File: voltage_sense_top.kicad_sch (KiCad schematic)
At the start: 42 parts, among them IC1 DAC101C081CIMK_NOPB, J1 Conn_Coaxial, J2 Conn_01x04, J4 HDMI_A, J5 Conn_Coaxial, U1 OPA188xxDBV, U2 ADA4000-1, U3 OPA188xxDBV, U4 MCP4017T-103E_LT, U5 OPA1641

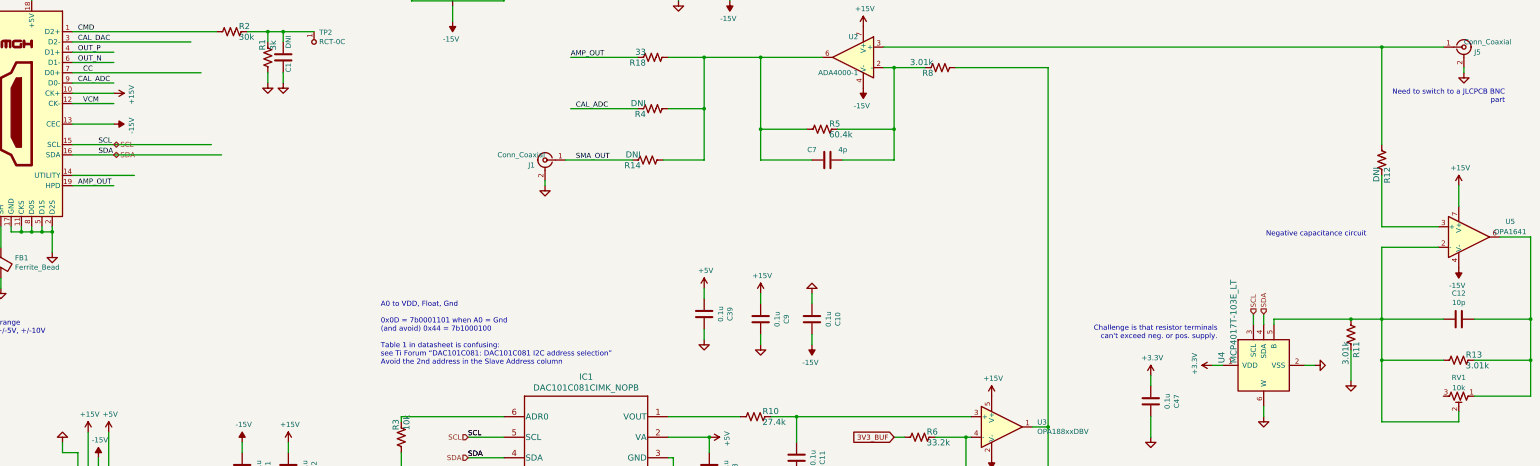
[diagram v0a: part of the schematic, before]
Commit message: found LCSC alternatives for some parts
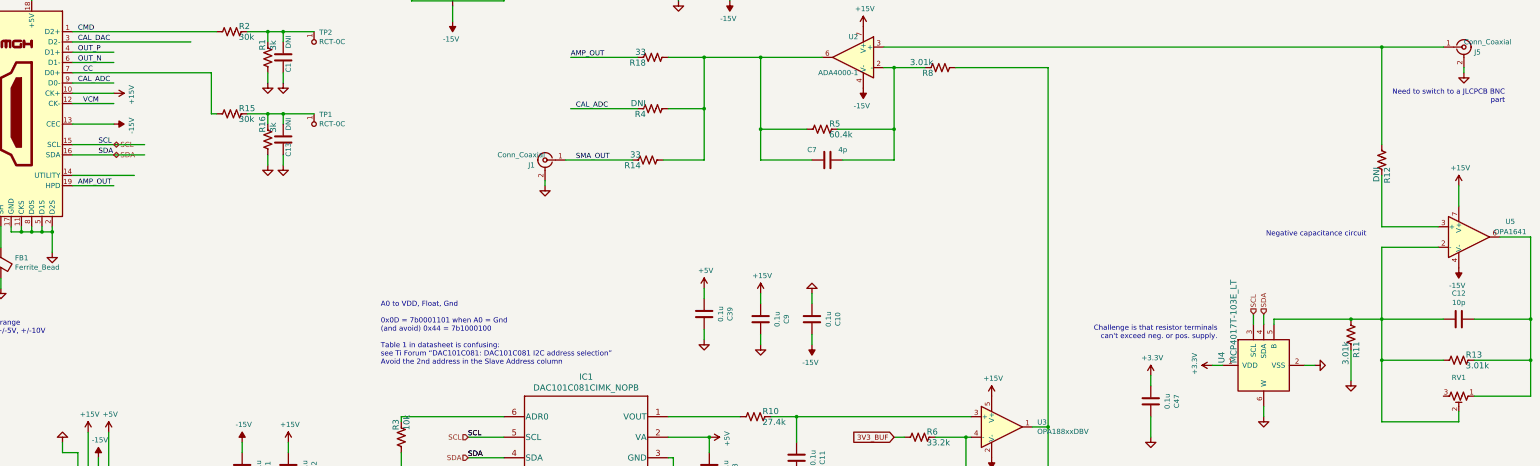
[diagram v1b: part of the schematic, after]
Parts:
- added C13: DNI, Capacitor_SMD:C_0603_1608Metric, symbol Device:C
- added R15: 30k, Resistor_SMD:R_0603_1608Metric, symbol Device:R_US
- added R16: 3k, Resistor_SMD:R_0603_1608Metric, symbol Device:R_US
- added TP1: RCT-0C, digikey-footprints:Test_Point_D1.02mm, symbol dk_Test-Points:RCT-0C
- J1: footprint covg-kicad:BU-SMA-G -> covg-kicad:SMA_HJ_SMA788
- R14: value DNI -> 33
- RV1: value 10k -> (none); footprint Potentiometer_SMD:Potentiometer_Bourns_3269W_Vertical -> (none)
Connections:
- net CC: now also R15.2
- net GND: now also C13.1, R16.2
- new net: C13.2, R15.1, R16.1, TP1.1
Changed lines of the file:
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@@
   (junction (at 200.66 158.75) (diameter 0) (color 0 0 0 0)
   )
+  (junction (at 91.44 63.5) (diameter 0) (color 0 0 0 0)
+  )
   (junction (at 246.38 52.07) (diameter 0) (color 0 0 0 0)
   )
+  (junction (at 95.25 63.5) (diameter 0) (color 0 0 0 0)
+  )
   (junction (at 284.48 158.75) (diameter 0) (color 0 0 0 0)
   )
@@
     (stroke (width 0) (type default) (color 0 0 0 0))
   )
+  (wire (pts (xy 91.44 66.04) (xy 91.44 63.5))
+    (stroke (width 0) (type default) (color 0 0 0 0))
+  )
   (wire (pts (xy 233.68 74.93) (xy 246.38 74.93))
     (stroke (width 0) (type default) (color 0 0 0 0))
@@
     (stroke (width 0) (type default) (color 0 0 0 0))
   )
+  (wire (pts (xy 95.25 76.2) (xy 95.25 73.66))
+    (stroke (width 0) (type default) (color 0 0 0 0))
+  )
   (wire (pts (xy 367.03 46.99) (xy 382.27 46.99))
     (stroke (width 0) (type default) (color 0 0 0 0))
@@
     (stroke (width 0) (type default) (color 0 0 0 0))
   )
-  (wire (pts (xy 43.18 73.66) (xy 80.01 73.66))
+  (wire (pts (xy 43.18 73.66) (xy 60.96 73.66))
     (stroke (width 0) (type default) (color 0 0 0 0))
   )
@@
     (stroke (width 0) (type default) (color 0 0 0 0))
   )
+  (wire (pts (xy 95.25 66.04) (xy 95.25 63.5))
+    (stroke (width 0) (type default) (color 0 0 0 0))
+  )
   (wire (pts (xy 284.48 158.75) (xy 284.48 161.29))
     (stroke (width 0) (type default) (color 0 0 0 0))
   )
-  (wire (pts (xy 43.18 53.34) (xy 74.93 53.34))
+  (wire (pts (xy 43.18 53.34) (xy 77.47 53.34))
     (stroke (width 0) (type default) (color 0 0 0 0))
   )
@@
     (stroke (width 0) (type default) (color 0 0 0 0))
   )
+  (wire (pts (xy 77.47 53.34) (xy 77.47 63.5))
+    (stroke (width 0) (type default) (color 0 0 0 0))
+  )
   (wire (pts (xy 284.48 158.75) (xy 284.48 140.97))
     (stroke (width 0) (type default) (color 0 0 0 0))
@@
     (stroke (width 0) (type default) (color 0 0 0 0))
   )
+  (wire (pts (xy 91.44 63.5) (xy 95.25 63.5))
+    (stroke (width 0) (type default) (color 0 0 0 0))
+  )
   (wire (pts (xy 205.74 35.56) (xy 205.74 33.02))
     (stroke (width 0) (type default) (color 0 0 0 0))
@@
     (stroke (width 0) (type default) (color 0 0 0 0))
   )
+  (wire (pts (xy 77.47 63.5) (xy 78.74 63.5))
+    (stroke (width 0) (type default) (color 0 0 0 0))
+  )
   (wire (pts (xy 127 35.56) (xy 149.86 35.56))
     (stroke (width 0) (type default) (color 0 0 0 0))
@@
     (stroke (width 0) (type default) (color 0 0 0 0))
   )
+  (wire (pts (xy 95.25 63.5) (xy 102.87 63.5))
+    (stroke (width 0) (type default) (color 0 0 0 0))
+  )
   (wire (pts (xy 367.03 96.52) (xy 367.03 114.3))
     (stroke (width 0) (type default) (color 0 0 0 0))
@@
     (stroke (width 0) (type default) (color 0 0 0 0))
   )
-  (wire (pts (xy 43.18 71.12) (xy 77.47 71.12))
+  (wire (pts (xy 43.18 71.12) (xy 60.96 71.12))
     (stroke (width 0) (type default) (color 0 0 0 0))
   )
@@
     (stroke (width 0) (type default) (color 0 0 0 0))
   )
+  (wire (pts (xy 91.44 76.2) (xy 91.44 73.66))
+    (stroke (width 0) (type default) (color 0 0 0 0))
+  )
   (wire (pts (xy 147.32 29.21) (xy 149.86 29.21))
     (stroke (width 0) (type default) (color 0 0 0 0))
@@
   )
   (wire (pts (xy 396.24 93.98) (xy 403.86 93.98))
+    (stroke (width 0) (type default) (color 0 0 0 0))
+  )
+  (wire (pts (xy 86.36 63.5) (xy 91.44 63.5))
     (stroke (width 0) (type default) (color 0 0 0 0))
   )
@@
     (pin "2")
   )
+  (symbol (lib_id "Device:R_US") (at 82.55 63.5 270) (unit 1)
+    (in_bom yes) (on_board yes)
+    (property "Reference" "R15" (id 0) (at 84.2772 62.1538 90)
+      (effects (font (size 1.4986 1.4986)) (justify left))
+    )
+    (property "Value" "30k" (id 1) (at 84.2772 64.8208 90)
+      (effects (font (size 1.4986 1.4986)) (justify left))
+    )
+    (property "Footprint" "Resistor_SMD:R_0603_1608Metric" (id 2) (at 82.55 63.5 0)
+      (effects (font (size 1.27 1.27)) hide)
+    )
+    (property "Datasheet" "" (id 3) (at 82.55 63.5 0)
+      (effects (font (size 1.27 1.27)) hide)
+    )
+    (property "Manf#" "" (id 4) (at 86.8172 62.1538 0)
+      (effects (font (size 1.27 1.27)) hide)
+    )
+    (property "Tolerance" "1%" (id 5) (at 82.55 63.5 0)
+      (effects (font (size 1.27 1.27)) hide)
+    )
+    (pin "1")
+    (pin "2")
+  )
   (symbol (lib_id "Device:C") (at 226.06 114.3 180) (unit 1)
     (in_bom yes) (on_board yes)
@@
       (effects (font (size 1.4986 1.4986)) (justify left))
     )
-    (property "Value" "DNI" (id 1) (at 183.6928 73.6092 90)
+    (property "Value" "33" (id 1) (at 183.6928 73.6092 90)
       (effects (font (size 1.4986 1.4986)) (justify left))
     )
@@
     (pin "2")
   )
+  (symbol (lib_id "power:GND") (at 95.25 76.2 0) (unit 1)
+    (in_bom yes) (on_board yes)
+    (property "Reference" "#PWR0136" (id 0) (at 95.25 82.55 0)
+      (effects (font (size 1.27 1.27)) hide)
+    )
+    (property "Value" "GND" (id 1) (at 95.377 79.4512 90)
+      (effects (font (size 1.27 1.27)) (justify right) hide)
+    )
+    (property "Footprint" "" (id 2) (at 95.25 76.2 0)
+      (effects (font (size 1.27 1.27)) hide)
+    )
+    (property "Datasheet" "" (id 3) (at 95.25 76.2 0)
+      (effects (font (size 1.27 1.27)) hide)
+    )
+    (pin "1")
+  )
   (symbol (lib_id "Device:R_US") (at 386.08 124.46 270) (unit 1)
     (in_bom yes) (on_board yes)
@@
     )
     (property "Tolerance" "1%" (id 5) (at 386.08 124.46 0)
+      (effects (font (size 1.27 1.27)) hide)
+    )
+    (pin "1")
+    (pin "2")
+  )
+  (symbol (lib_id "Device:R_US") (at 91.44 69.85 0) (unit 1)
+    (in_bom yes) (on_board yes)
+    (property "Reference" "R16" (id 0) (at 90.0938 68.1228 90)
+      (effects (font (size 1.4986 1.4986)) (justify left))
+    )
+    (property "Value" "3k" (id 1) (at 92.7608 68.1228 90)
+      (effects (font (size 1.4986 1.4986)) (justify left))
+    )
+    (property "Footprint" "Resistor_SMD:R_0603_1608Metric" (id 2) (at 91.44 69.85 0)
+      (effects (font (size 1.27 1.27)) hide)
+    )
+    (property "Datasheet" "" (id 3) (at 91.44 69.85 0)
+      (effects (font (size 1.27 1.27)) hide)
+    )
+    (property "Manf#" "RC0603FR-073KL" (id 4) (at 90.0938 65.5828 0)
+      (effects (font (size 1.27 1.27)) hide)
+    )
+    (property "Tolerance" "1%" (id 5) (at 91.44 69.85 0)
       (effects (font (size 1.27 1.27)) hide)
     )
@@
     (in_bom yes) (on_board yes) (fields_autoplaced)
     (property "Reference" "RV1" (id 0) (at 386.08 128.7612 90))
-    (property "Value" "10k" (id 1) (at 386.08 131.2981 90))
-    (property "Footprint" "Potentiometer_SMD:Potentiometer_Bourns_3269W_Vertical" (id 2) (at 386.08 133.35 0)
+    (property "Value" "" (id 1) (at 386.08 131.2981 90))
+    (property "Footprint" "" (id 2) (at 386.08 133.35 0)
       (effects (font (size 1.27 1.27)) hide)
     )
@@
       (effects (font (size 1.27 1.27)) (justify left))
     )
-    (property "Footprint" "covg-kicad:BU-SMA-G" (id 2) (at 160.02 74.93 0)
+    (property "Footprint" "covg-kicad:SMA_HJ_SMA788" (id 2) (at 160.02 74.93 0)
       (effects (font (size 1.27 1.27)) hide)
     )
@@
     (pin "1")
   )
+  (symbol (lib_id "Device:C") (at 95.25 69.85 180) (unit 1)
+    (in_bom yes) (on_board yes)
+    (property "Reference" "C13" (id 0) (at 96.52 72.39 90))
+    (property "Value" "DNI" (id 1) (at 96.52 66.04 90))
+    (property "Footprint" "Capacitor_SMD:C_0603_1608Metric" (id 2) (at 94.2848 66.04 0)
+      (effects (font (size 1.27 1.27)) hide)
+    )
+    (property "Datasheet" "~" (id 3) (at 95.25 69.85 0)
+      (effects (font (size 1.27 1.27)) hide)
+    )
+    (property "Manf#" "CC0603JRNPO9BN100" (id 4) (at 101.6508 72.39 0)
+      (effects (font (size 1.27 1.27)) hide)
+    )
+    (property "Tolerance" "5%" (id 5) (at 101.6508 72.39 0)
+      (effects (font (size 1.27 1.27)) hide)
+    )
+    (property "voltage" "50V" (id 6) (at 101.6508 72.39 0)
+      (effects (font (size 1.27 1.27)) hide)
+    )
+    (pin "1")
+    (pin "2")
+  )
   (symbol (lib_id "power:GND") (at 222.25 158.75 0) (unit 1)
     (in_bom yes) (on_board yes)
@@
     (pin "6")
   )
+  (symbol (lib_id "power:GND") (at 91.44 76.2 0) (unit 1)
+    (in_bom yes) (on_board yes)
+    (property "Reference" "#PWR0125" (id 0) (at 91.44 82.55 0)
+      (effects (font (size 1.27 1.27)) hide)
+    )
+    (property "Value" "GND" (id 1) (at 91.567 79.4512 90)
+      (effects (font (size 1.27 1.27)) (justify right) hide)
+    )
+    (property "Footprint" "" (id 2) (at 91.44 76.2 0)
+      (effects (font (size 1.27 1.27)) hide)
+    )
+    (property "Datasheet" "" (id 3) (at 91.44 76.2 0)
+      (effects (font (size 1.27 1.27)) hide)
+    )
+    (pin "1")
+  )
   (symbol (lib_id "power:GND") (at 350.52 125.73 90) (unit 1)
     (in_bom yes) (on_board yes)
@@
     (pin "2")
   )
+  (symbol (lib_id "dk_Test-Points:RCT-0C") (at 102.87 66.04 0) (unit 1)
+    (in_bom yes) (on_board yes)
+    (property "Reference" "TP1" (id 0) (at 104.14 63.6778 0)
+      (effects (font (size 1.27 1.27)) (justify left))
+    )
+    (property "Value" "RCT-0C" (id 1) (at 104.14 65.9892 0)
+      (effects (font (size 1.27 1.27)) (justify left))
+    )
+    (property "Footprint" "digikey-footprints:Test_Point_D1.02mm" (id 2) (at 107.95 60.96 0)
+      (effects (font (size 1.524 1.524)) (justify left) hide)
+    )
+    (property "Datasheet" "https://www.te.com/commerce/DocumentDelivery/DDEController?Action=srchrtrv&DocNm=1773266&DocType=DS&DocLang=English" (id 3) (at 107.95 58.42 0)
+      (effects (font (size 1.524 1.524)) (justify left) hide)
+    )
+    (pin "1")
+  )
   (symbol (lib_id "Device:C") (at 213.36 114.3 180) (unit 1)
